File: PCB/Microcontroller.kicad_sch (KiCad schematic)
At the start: 22 parts, among them SW1 SW_DIP_x01, U1 RP2040, U2 W25Q128JV, Y1 Crystal

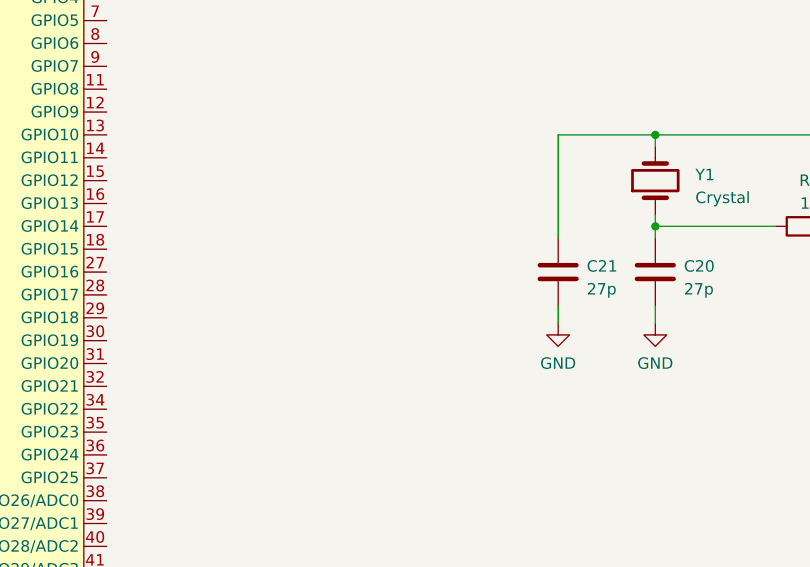
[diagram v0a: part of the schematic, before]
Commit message: uc sheet modified
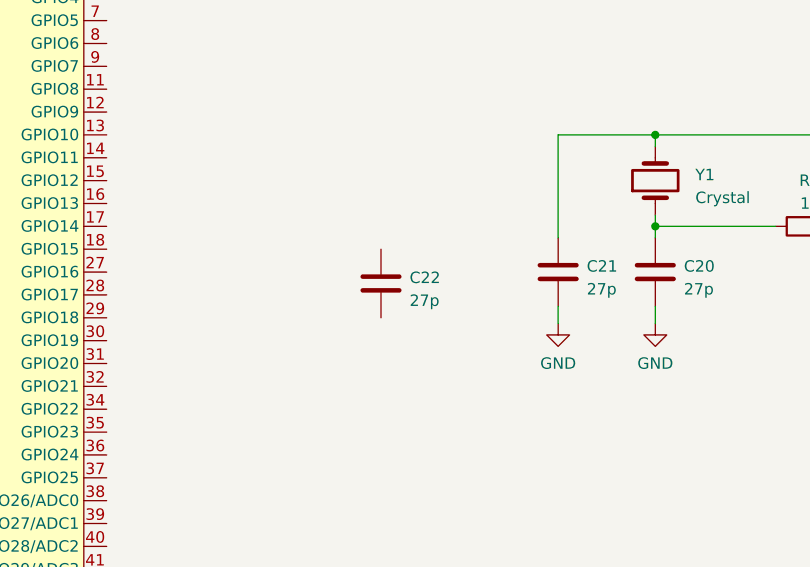
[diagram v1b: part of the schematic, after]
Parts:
- added C22: 27p, symbol Device:C
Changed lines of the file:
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@@
+    )
+  )
+  (symbol (lib_id "Device:C") (at 202.565 113.665 0) (unit 1)
+    (in_bom yes) (on_board yes) (dnp no) (fields_autoplaced)
+    (property "Reference" "C22" (at 205.74 113.03 0)
+      (effects (font (size 1.27 1.27)) (justify left))
+    )
+    (property "Value" "27p" (at 205.74 115.57 0)
+      (effects (font (size 1.27 1.27)) (justify left))
+    )
+    (property "Footprint" "" (at 203.5302 117.475 0)
+      (effects (font (size 1.27 1.27)) hide)
+    )
+    (property "Datasheet" "~" (at 202.565 113.665 0)
+      (effects (font (size 1.27 1.27)) hide)
+    )
+    (pin "1")
+    (pin "2")
+    (instances
+      (project "Raspi Pico Board"
+        (path "/74fd863b-9e5a-408c-8bbe-ce93005c4fd4/33b17cad-1f6d-4a95-bb1b-2afc5c71b563"
+          (reference "C22") (unit 1)
+        )
+      )
     )
   )

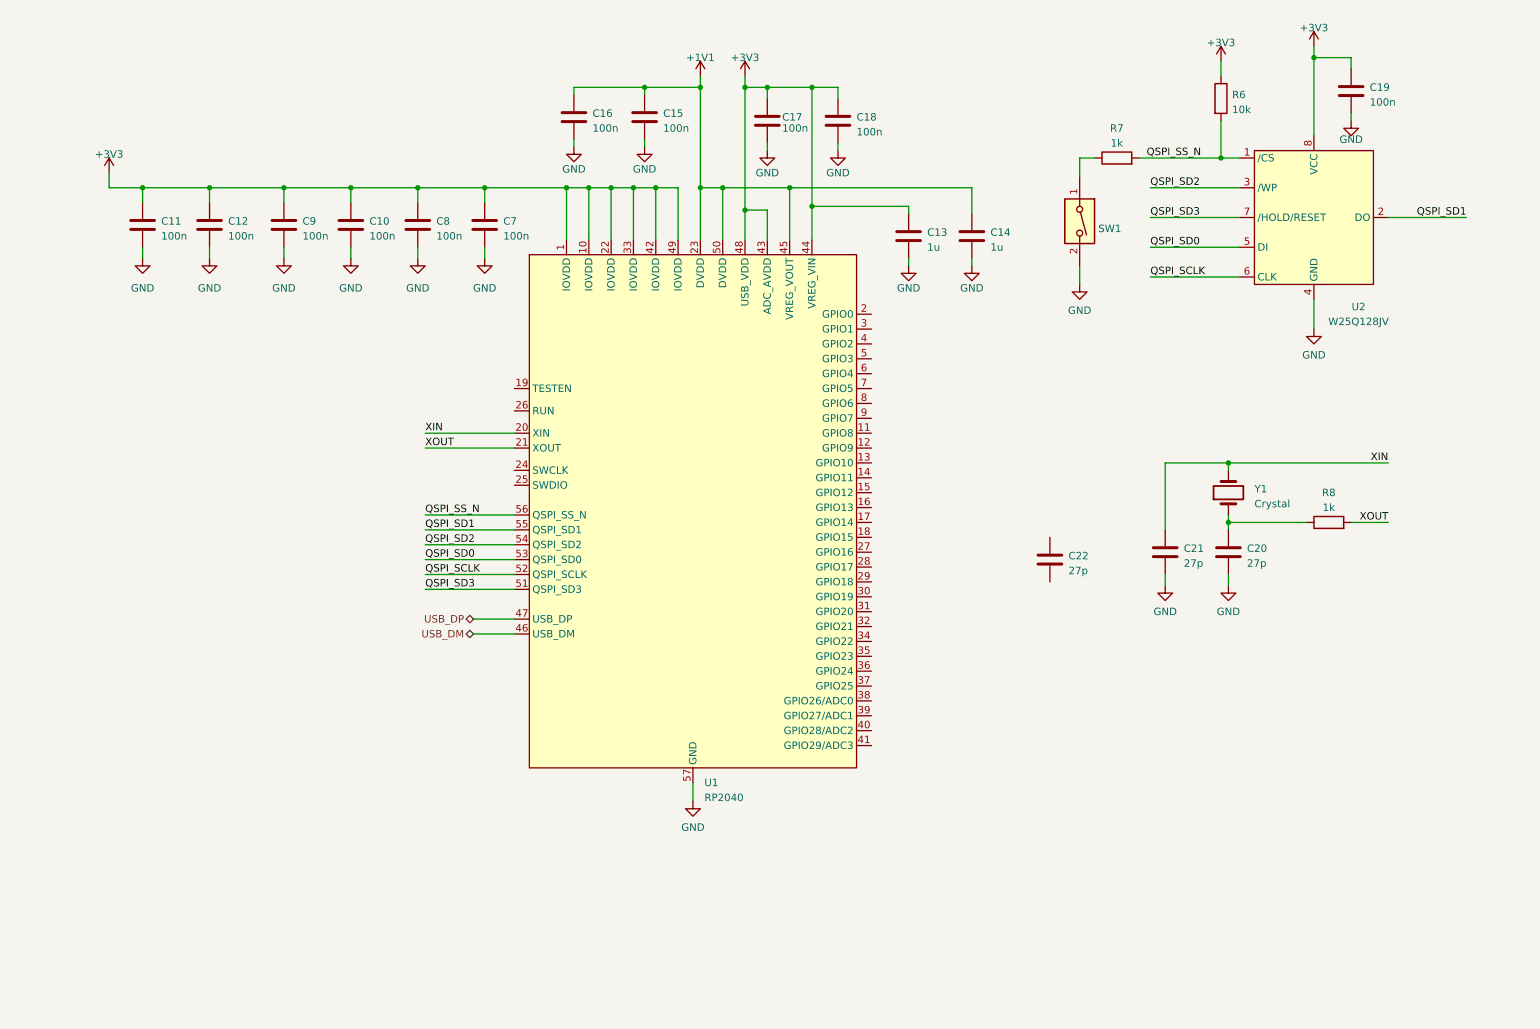
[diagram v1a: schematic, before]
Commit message: New sheet added
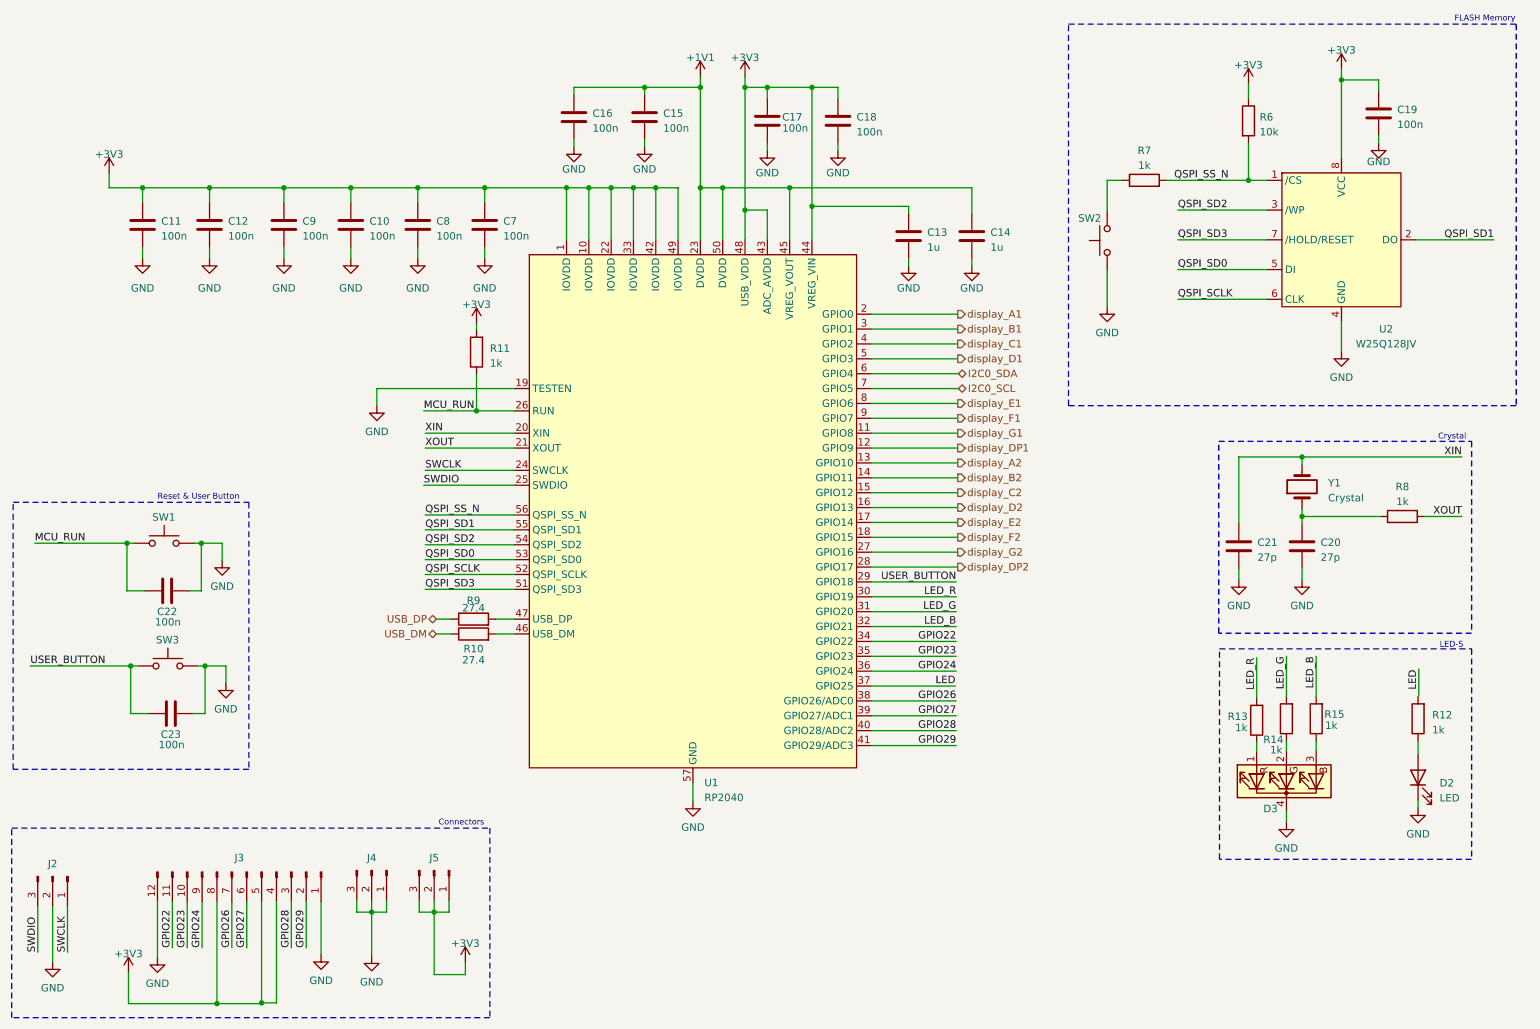
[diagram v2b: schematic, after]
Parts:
- removed SW1: SW_DIP_x01, symbol Switch:SW_DIP_x01
- added C23: 100n, symbol Device:C
- added D2: LED, symbol Device:LED
- added D3: LED_RGBK, symbol Device:LED_RGBK
- added J2, J4, J5: Conn_01x03_Pin, symbol Connector:Conn_01x03_Pin
- added J3: Conn_01x12_Pin, symbol Connector:Conn_01x12_Pin
- added R10, R9: 27.4, symbol Device:R
- added R11, R12, R13, R14, R15: 1k, symbol Device:R
- added SW1, SW2, SW3: SW_Push, symbol Switch:SW_Push
- C22: value 27p -> 100n
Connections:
- net +3V3: now also J3.4 (Pin_4), J3.5 (Pin_5), J3.8 (Pin_8), J5.1 (Pin_1), J5.2 (Pin_2), J5.3 (Pin_3), R11.2
- net GND: now also C22.1, U1.19 (TESTEN), C23.1, D2.1 (K), D3.4 (K), J2.2 (Pin_2), J3.1 (Pin_1), J3.12 (Pin_12), J4.1 (Pin_1), J4.2 (Pin_2), J4.3 (Pin_3), SW1.2, SW2.1, SW3.2
- net USB_DM: now also R10.1; no longer U1.46 (USB_DM)
- net USB_DP: now also R9.1; no longer U1.47 (USB_DP)
- net at R7.1: now also SW2.2
- net MCU_RUN: now reaches C22.2
- net MCU_RUN: now also U1.26 (RUN), R11.1, SW1.1
- net display_G1: now reaches U1.11 (GPIO8)
- net display_DP1: now reaches U1.12 (GPIO9)
- net display_A2: now reaches U1.13 (GPIO10)
- net display_B2: now reaches U1.14 (GPIO11)
- net display_C2: now reaches U1.15 (GPIO12)
- net display_D2: now reaches U1.16 (GPIO13)
- net display_E2: now reaches U1.17 (GPIO14)
- net display_F2: now reaches U1.18 (GPIO15)
- net display_A1: now reaches U1.2 (GPIO0)
- net SWCLK: now reaches U1.24 (SWCLK)
- net SWCLK: now also J2.1 (Pin_1)
- net SWDIO: now reaches U1.25 (SWDIO)
- net SWDIO: now also J2.3 (Pin_3)
- net display_G2: now reaches U1.27 (GPIO16)
- net display_DP2: now reaches U1.28 (GPIO17)
- net USER_BUTTON: now reaches U1.29 (GPIO18)
- net USER_BUTTON: now also C23.2, SW3.1
- net display_B1: now reaches U1.3 (GPIO1)
- net LED_R: now reaches U1.30 (GPIO19)
- net LED_R: now also R13.2
- net LED_G: now reaches U1.31 (GPIO20)
- net LED_G: now also R14.2
- net LED_B: now reaches U1.32 (GPIO21)
- net LED_B: now also R15.2
- net GPIO22: now reaches U1.34 (GPIO22)
- net GPIO22: now also J3.11 (Pin_11)
- net GPIO23: now reaches U1.35 (GPIO23)
- net GPIO23: now also J3.10 (Pin_10)
- net GPIO24: now reaches U1.36 (GPIO24)
- net GPIO24: now also J3.9 (Pin_9)
- net LED: now reaches U1.37 (GPIO25)
- net GPIO26: now reaches U1.38 (GPIO26/ADC0)
- net GPIO26: now also J3.7 (Pin_7)
- net GPIO27: now reaches U1.39 (GPIO27/ADC1)
- net GPIO27: now also J3.6 (Pin_6)
- net display_C1: now reaches U1.4 (GPIO2)
- net GPIO28: now reaches U1.40 (GPIO28/ADC2)
- net GPIO28: now also J3.3 (Pin_3)
- net GPIO29: now reaches U1.41 (GPIO29/ADC3)
- net GPIO29: now also J3.2 (Pin_2)
- net display_D1: now reaches U1.5 (GPIO3)
- net I2C0_SDA: now reaches U1.6 (GPIO4)
- net I2C0_SCL: now reaches U1.7 (GPIO5)
- net display_E1: now reaches U1.8 (GPIO6)
- net display_F1: now reaches U1.9 (GPIO7)
- new net: D3.2 (GA), R14.1
- new net: D2.2 (A), R12.1
- new net: D3.3 (BA), R15.1
- new net: D3.1 (RA), R13.1
- new net: R9.2, U1.47 (USB_DP)
- new net: R10.2, U1.46 (USB_DM)
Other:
- note added: "Connectors"
- note added: "Crystal"
- note added: "FLASH Memory"
- note added: "LED-S"
- note added: "Reset & User Button"
- moved on the sheet: C19, C20, C21, R6, R7, R8, U2, Y1

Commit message: Layout complted, gerber files generated
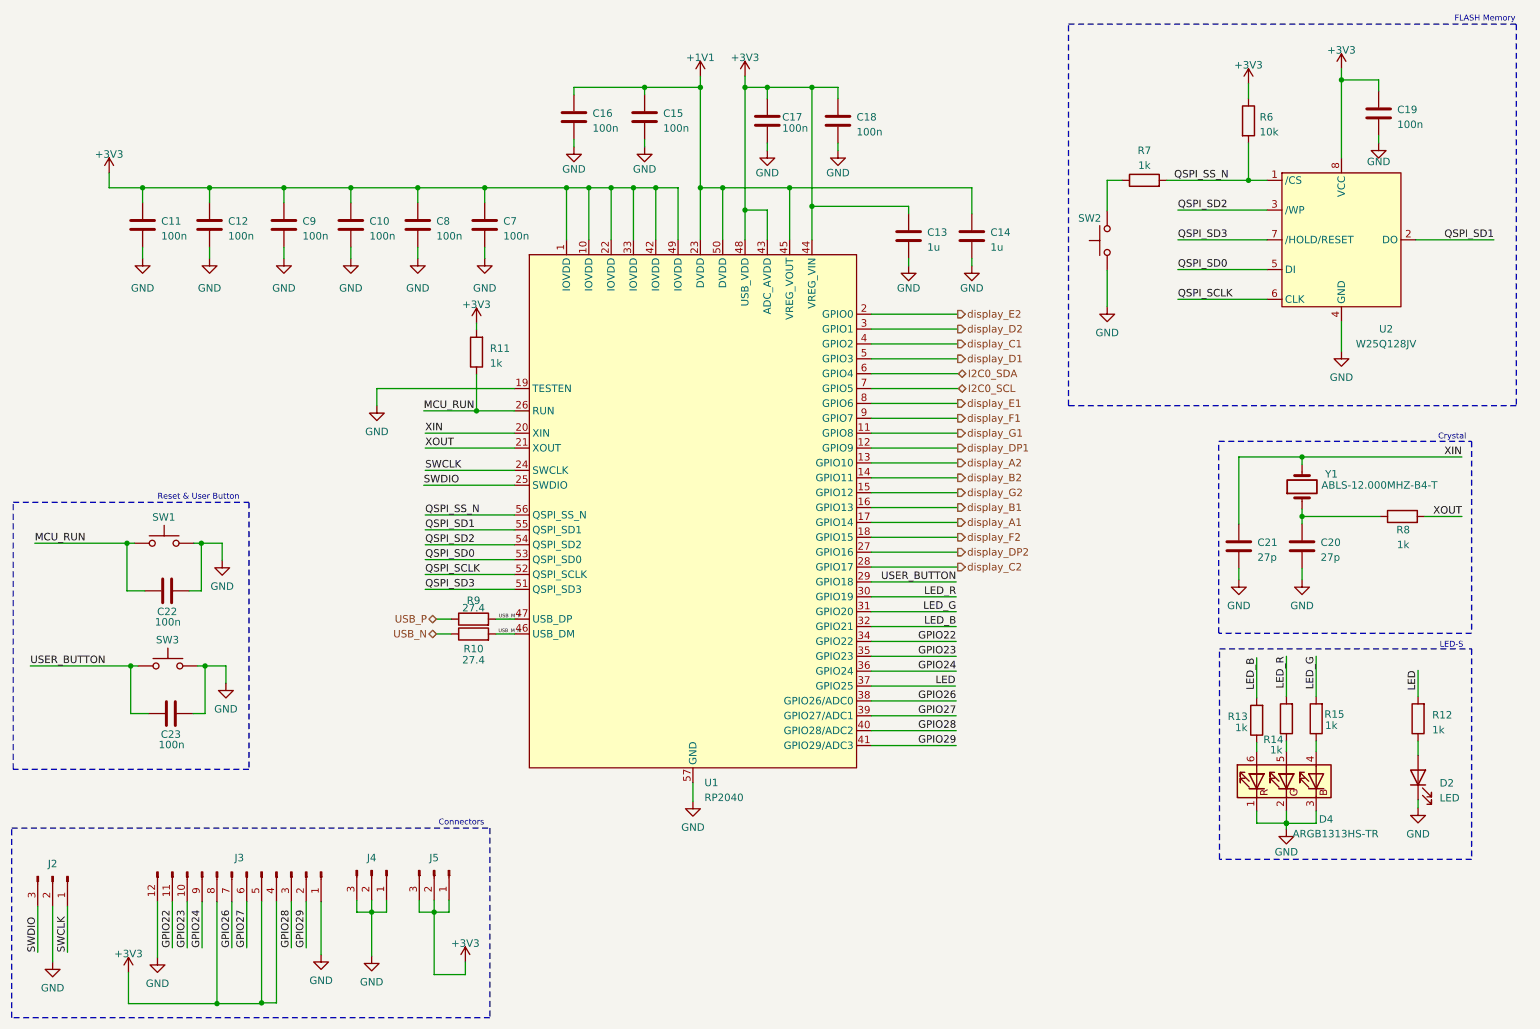
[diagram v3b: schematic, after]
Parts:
- removed D3: LED_RGBK, symbol Device:LED_RGBK
- added D4: ARGB1313HS-TR, User_Footprint:RGB_ARGB1313HS-TR, symbol Device:LED_RGB
- C10, C11, C12, C13, C14, C15, C16, C17, C18, C19, C20, C21, C22, C23, C7, C8, C9: footprint (none) -> Capacitor_SMD:C_0603_1608Metric
- D2: footprint (none) -> LED_SMD:LED_0805_2012Metric
- J2, J4, J5: footprint (none) -> Connector_PinHeader_2.54mm:PinHeader_1x03_P2.54mm_Vertical
- J3: footprint (none) -> Connector_PinHeader_2.54mm:PinHeader_1x12_P2.54mm_Vertical
- R10, R11, R12, R13, R14, R15, R6, R7, R8, R9: footprint (none) -> Resistor_SMD:R_0603_1608Metric
- SW1, SW2, SW3: footprint (none) -> Button_Switch_SMD:SW_SPST_B3U-1000P
- U1: footprint (none) -> Package_DFN_QFN:QFN-56-1EP_7x7mm_P0.4mm_EP3.2x3.2mm
- U2: footprint (none) -> Package_SON:WSON-8-1EP_6x5mm_P1.27mm_EP3.4x4.3mm
- Y1: value Crystal -> ABLS-12.000MHZ-B4-T; footprint (none) -> User_Footprint:ABLS-12.000MHZ-B4-T
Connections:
- net GND: now also D4.1 (RK), D4.2 (GK), D4.3 (BK)
- net LED: now also R12.2
- net LED_B: now also R13.2; no longer R15.2
- net LED_G: now also R15.2; no longer R14.2
- net LED_R: now also R14.2; no longer R13.2
- net display_A1: now also U1.17 (GPIO14); no longer U1.2 (GPIO0)
- net display_B1: now also U1.16 (GPIO13); no longer U1.3 (GPIO1)
- net display_C2: now also U1.28 (GPIO17); no longer U1.15 (GPIO12)
- net display_D2: now also U1.3 (GPIO1); no longer U1.16 (GPIO13)
- net display_DP2: now also U1.27 (GPIO16); no longer U1.28 (GPIO17)
- net display_E2: now also U1.2 (GPIO0); no longer U1.17 (GPIO14)
- net display_G2: now also U1.15 (GPIO12); no longer U1.27 (GPIO16)
- net at R14.1: now also D4.5 (GA)
- net at R15.1: now also D4.4 (BA)
- net at R13.1: now also D4.6 (RA)
- net USB_M_P: now reaches R9.2, U1.47 (USB_DP)
- net USB_M_N: now reaches R10.2, U1.46 (USB_DM)
- net USB_DM renamed USB_N
- net USB_DP renamed USB_P
